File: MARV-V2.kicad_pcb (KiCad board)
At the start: 4 copper layers, 50.7 x 45.5 mm, 106 parts, among them J10 DBG pads (SWCLK SWDIO GND), J11 microSD, Molex 104031-0811 pu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, J3 ESC pads (CURR TX M4 M3 M2 M1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, J4 USB_C_PROGRAM_POWER, J6 IO array signal column (inner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, J7 IO array power column (5V / 3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, J8 IO array GND column (board ed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, Q1 AO3401A, SW1 RESET (RUN to GND), SW2 BOOTSEL (via R24), U12 TPS7A2033PDBVR, U20 RP2354B, U21 ICM-45686 6-axis IMU, U22 BMP581 barometer, U23 ADXL375 high-g accelerometer, U24 DNP: W25Q32JVSNIQ, 32 Mbit QS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, U7 AP63203WU-7, Y1 12 MHz TAXM12M4RFBCCT2T, CL 1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

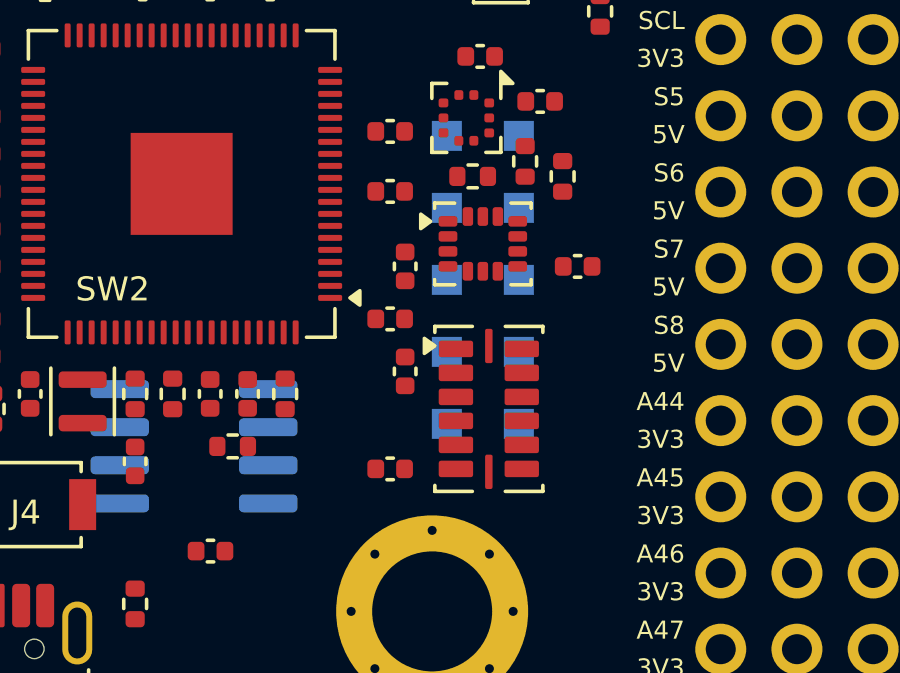
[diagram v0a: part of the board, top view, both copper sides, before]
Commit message: Save communication schematic, locking microSD and manual PCB updates
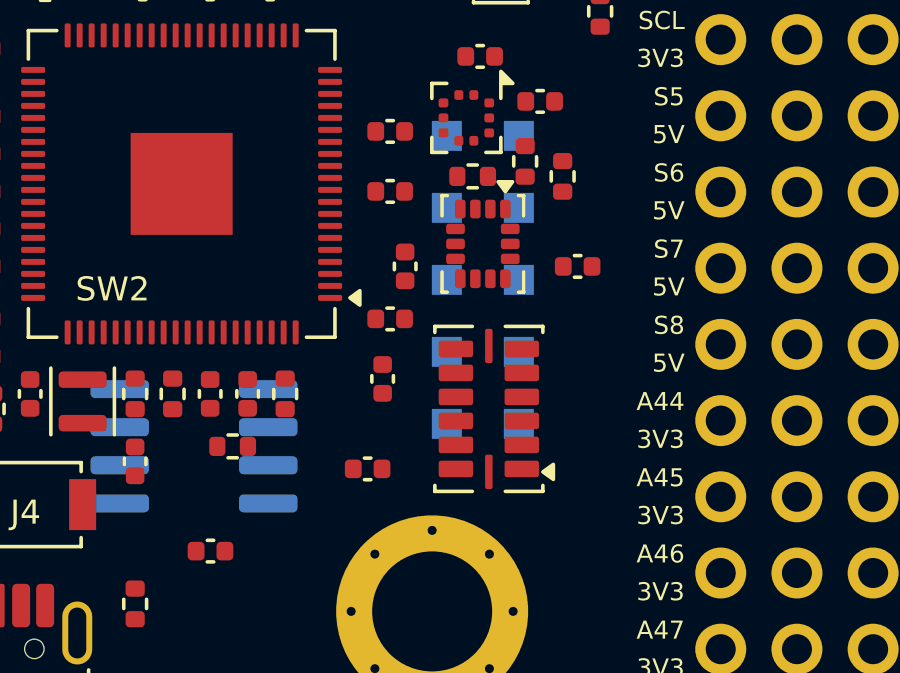
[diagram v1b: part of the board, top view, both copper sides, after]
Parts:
- moved C60 0.79 mm to (107.5, 107.5)
- moved C59 0.75 mm to (107.0, 110.5)
- turned U21 to -90 degrees
- turned U23 to 180 degrees
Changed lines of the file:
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@@
 	(footprint "Capacitor_SMD:C_0402_1005Metric"
 		(layer "F.Cu")
-		(at 108.25 107.25 -90)
+		(at 107.5 107.5 -90)
 		(descr "Capacitor SMD 0402 (1005 Metric), square (rectangular) end terminal, IPC-7351 nominal, (Body size source: IPC-SM-782 page 76, https://www.pcb-3d.com/wordpress/wp-content/uploads/ipc-sm-782a_amendment_1_and_2.pdf)")
 		(tags "capacitor")
@@
 		)
 		(embedded_fonts no)
-		(model "${KIPRJMOD}/MARV_Packages.3dshapes/microSD_HC_Molex_104031-0811.step"
+		(model "${KIPRJMOD}/MARV_Packages.3dshapes/microSD_HC_Molex_47219-2001.step"
 			(offset
-				(xyz 0.092 -0.3 1.4456)
+				(xyz -0.005 0 0)
 			)
 			(scale
@@
 			)
 			(rotate
-				(xyz -90 0 180)
+				(xyz 0 0 180)
 			)
 		)
@@
 	(footprint "MARV_Packages:InvenSense_LGA-14_2.5x3mm_P0.5mm_ICM45686"
 		(layer "F.Cu")
-		(at 110.84 103)
+		(at 110.84 103 -90)
 		(descr "TDK InvenSense ICM-45686 6-axis IMU, 14-pin LGA 2.5x3x0.81 mm, 0.5 mm pitch. Pad geometry identical to KiCad LGA-14_3x2.5mm_P0.5mm_LayoutBorder3x4y and verified by the lead against DS-000577 Rev 1.0 Sec 11.2 (page 52 TOP VIEW: pin 1 at top of the left edge, counterclockwise; side columns x=+/-1.1625, top/bottom rows y=+/-0.9125). 3D model is a dimensional stand-in copied from the KiCad generic LGA-14 STEP.")
 		(tags "InvenSense TDK ICM-45686 LGA-14 IMU accelerometer gyroscope")
 		(property "Reference" "U21"
-			(at 0 -2.2 0)
+			(at 0 -2.2 90)
 			(layer "F.SilkS")
 			(hide yes)
@@
 		)
 		(property "Value" "ICM-45686 6-axis IMU"
-			(at 0 2.2 0)
+			(at 0 2.2 90)
 			(layer "F.Fab")
 			(hide yes)
@@
 		)
 		(property "Datasheet" ""
-			(at 0 0 0)
+			(at 0 0 90)
 			(layer "F.Fab")
 			(hide yes)
@@
 		)
 		(property "Description" ""
-			(at 0 0 0)
+			(at 0 0 90)
 			(layer "F.Fab")
 			(hide yes)
@@
 		)
 		(property "KiLib_Generator" "package/no_lead"
-			(at 0 0 0)
+			(at 0 0 90)
 			(layer "F.SilkS")
 			(hide yes)
@@
 		(duplicate_pad_numbers_are_jumpers no)
 		(fp_line
-			(start -1.61 -1.36)
-			(end -0.935 -1.36)
+			(start -1.61 1.36)
+			(end -1.61 1.185)
 			(stroke
 				(width 0.12)
@@
 		)
 		(fp_line
-			(start -1.61 -1.185)
-			(end -1.61 -1.36)
+			(start -0.935 1.36)
+			(end -1.61 1.36)
 			(stroke
 				(width 0.12)
@@
 		)
 		(fp_line
-			(start -1.61 1.36)
-			(end -1.61 1.185)
+			(start 1.61 1.36)
+			(end 0.935 1.36)
 			(stroke
 				(width 0.12)
@@
 		)
 		(fp_line
-			(start -0.935 1.36)
-			(end -1.61 1.36)
+			(start 1.61 1.185)
+			(end 1.61 1.36)
 			(stroke
 				(width 0.12)
@@
 		)
 		(fp_line
-			(start 0.935 -1.36)
-			(end 1.61 -1.36)
+			(start -1.61 -1.185)
+			(end -1.61 -1.36)
 			(stroke
 				(width 0.12)
@@
 		)
 		(fp_line
-			(start 1.61 -1.36)
-			(end 1.61 -1.185)
+			(start -1.61 -1.36)
+			(end -0.935 -1.36)
 			(stroke
 				(width 0.12)
@@
 		)
 		(fp_line
-			(start 1.61 1.185)
-			(end 1.61 1.36)
+			(start 0.935 -1.36)
+			(end 1.61 -1.36)
 			(stroke
 				(width 0.12)
@@
 		)
 		(fp_line
-			(start 1.61 1.36)
-			(end 0.935 1.36)
+			(start 1.61 -1.36)
+			(end 1.61 -1.185)
 			(stroke
 				(width 0.12)
@@
 		)
 		(fp_text user "${REFERENCE}"
-			(at 0 0 0)
+			(at 0 0 90)
 			(layer "F.Fab")
 			(effects
@@
 		)
 		(pad "1" smd roundrect
-			(at -1.1625 -0.75)
+			(at -1.1625 -0.75 270)
 			(size 0.625 0.35)
 			(layers "F.Cu" "F.Mask" "F.Paste")
@@
 		)
 		(pad "2" smd roundrect
-			(at -1.1625 -0.25)
+			(at -1.1625 -0.25 270)
 			(size 0.625 0.35)
 			(layers "F.Cu" "F.Mask" "F.Paste")
@@
 		)
 		(pad "3" smd roundrect
-			(at -1.1625 0.25)
+			(at -1.1625 0.25 270)
 			(size 0.625 0.35)
 			(layers "F.Cu" "F.Mask" "F.Paste")
@@
 		)
 		(pad "4" smd roundrect
-			(at -1.1625 0.75)
+			(at -1.1625 0.75 270)
 			(size 0.625 0.35)
 			(layers "F.Cu" "F.Mask" "F.Paste")
@@
 		)
 		(pad "5" smd roundrect
-			(at -0.5 0.9125)
+			(at -0.5 0.9125 270)
 			(size 0.35 0.625)
 			(layers "F.Cu" "F.Mask" "F.Paste")
@@
 		)
 		(pad "6" smd roundrect
-			(at 0 0.9125)
+			(at 0 0.9125 270)
 			(size 0.35 0.625)
 			(layers "F.Cu" "F.Mask" "F.Paste")
@@
 		)
 		(pad "7" smd roundrect
-			(at 0.5 0.9125)
+			(at 0.5 0.9125 270)
 			(size 0.35 0.625)
 			(layers "F.Cu" "F.Mask" "F.Paste")
@@
 		)
 		(pad "8" smd roundrect
-			(at 1.1625 0.75)
+			(at 1.1625 0.75 270)
 			(size 0.625 0.35)
 			(layers "F.Cu" "F.Mask" "F.Paste")
@@
 		)
 		(pad "9" smd roundrect
-			(at 1.1625 0.25)
+			(at 1.1625 0.25 270)
 			(size 0.625 0.35)
 			(layers "F.Cu" "F.Mask" "F.Paste")
@@
 		)
 		(pad "10" smd roundrect
-			(at 1.1625 -0.25)
+			(at 1.1625 -0.25 270)
 			(size 0.625 0.35)
 			(layers "F.Cu" "F.Mask" "F.Paste")
@@
 		)
 		(pad "11" smd roundrect
-			(at 1.1625 -0.75)
+			(at 1.1625 -0.75 270)
 			(size 0.625 0.35)
 			(layers "F.Cu" "F.Mask" "F.Paste")
@@
 		)
 		(pad "12" smd roundrect
-			(at 0.5 -0.9125)
+			(at 0.5 -0.9125 270)
 			(size 0.35 0.625)
 			(layers "F.Cu" "F.Mask" "F.Paste")
@@
 		)
 		(pad "13" smd roundrect
-			(at 0 -0.9125)
+			(at 0 -0.9125 270)
 			(size 0.35 0.625)
 			(layers "F.Cu" "F.Mask" "F.Paste")
@@
 		)
 		(pad "14" smd roundrect
-			(at -0.5 -0.9125)
+			(at -0.5 -0.9125 270)
 			(size 0.35 0.625)
 			(layers "F.Cu" "F.Mask" "F.Paste")
@@
 	(footprint "MARV_Packages:Analog_LGA-14_3x5mm_P0.8mm_ADXL375"
 		(layer "F.Cu")
-		(at 111.039999 108.5)
+		(at 111.039999 108.5 180)
 		(descr "Analog Devices ADXL375, CC-14-1 14-terminal 3x5 mm LGA; datasheet recommended land pattern")
 		(tags "Analog Devices ADXL375 LGA-14 accelerometer")
@@
 		(duplicate_pad_numbers_are_jumpers no)
 		(fp_line
-			(start -1.8 -2.75)
-			(end -1.8 -2.55)
+			(start 1.8 2.75)
+			(end 1.8 2.55)
 			(stroke
 				(width 0.12)
@@
 		)
 		(fp_line
-			(start -1.8 -2.75)
-			(end -0.55 -2.75)
+			(start 1.8 -2.75)
+			(end 1.8 -2.55)
 			(stroke
 				(width 0.12)
@@
 		)
 		(fp_line
-			(start -1.8 2.75)
-			(end -1.8 2.55)
+			(start 0.55 2.75)
+			(end 1.8 2.75)
 			(stroke
 				(width 0.12)
@@
 		)
 		(fp_line
-			(start -1.8 2.75)
-			(end -0.55 2.75)
+			(start 0.55 -2.75)
+			(end 1.8 -2.75)
 			(stroke
 				(width 0.12)
@@
 		)
 		(fp_line
-			(start 0.55 -2.75)
-			(end 1.8 -2.75)
+			(start -1.8 2.75)
+			(end -0.55 2.75)
 			(stroke
 				(width 0.12)
@@
 		)
 		(fp_line
-			(start 0.55 2.75)
-			(end 1.8 2.75)
+			(start -1.8 2.75)
+			(end -1.8 2.55)
 			(stroke
 				(width 0.12)
@@
 		)
 		(fp_line
-			(start 1.8 -2.75)
-			(end 1.8 -2.55)
+			(start -1.8 -2.75)
+			(end -0.55 -2.75)
 			(stroke
 				(width 0.12)
@@
 		)
 		(fp_line
-			(start 1.8 2.75)
-			(end 1.8 2.55)
+			(start -1.8 -2.75)
+			(end -1.8 -2.55)
 			(stroke
 				(width 0.12)
@@
 		)
 		(pad "1" smd roundrect
-			(at -1.0975 -2)
+			(at -1.0975 -2 180)
 			(size 1.145 0.55)
 			(layers "F.Cu" "F.Mask" "F.Paste")
@@
 		)
 		(pad "2" smd roundrect
-			(at -1.0975 -1.2)
+			(at -1.0975 -1.2 180)
 			(size 1.145 0.55)
 			(layers "F.Cu" "F.Mask" "F.Paste")
@@
 		)
 		(pad "3" smd roundrect
-			(at -1.0975 -0.4)
+			(at -1.0975 -0.4 180)
 			(size 1.145 0.55)
 			(layers "F.Cu" "F.Mask" "F.Paste")
@@
 		)
 		(pad "4" smd roundrect
-			(at -1.0975 0.4)
+			(at -1.0975 0.4 180)
 			(size 1.145 0.55)
 			(layers "F.Cu" "F.Mask" "F.Paste")
@@
 		)
 		(pad "5" smd roundrect
-			(at -1.0975 1.2)
+			(at -1.0975 1.2 180)
 			(size 1.145 0.55)
 			(layers "F.Cu" "F.Mask" "F.Paste")
@@
 		)
 		(pad "6" smd roundrect
-			(at -1.0975 2)
+			(at -1.0975 2 180)
 			(size 1.145 0.55)
 			(layers "F.Cu" "F.Mask" "F.Paste")
@@
 		)
 		(pad "7" smd roundrect
-			(at 0 2.0975)
+			(at 0 2.0975 180)
 			(size 0.25 1.145)
 			(layers "F.Cu" "F.Mask" "F.Paste")
@@
 		)
 		(pad "8" smd roundrect
-			(at 1.0975 2)
+			(at 1.0975 2 180)
 			(size 1.145 0.55)
 			(layers "F.Cu" "F.Mask" "F.Paste")
@@
 		)
 		(pad "9" smd roundrect
-			(at 1.0975 1.2)
+			(at 1.0975 1.2 180)
 			(size 1.145 0.55)
 			(layers "F.Cu" "F.Mask" "F.Paste")
@@
 		)
 		(pad "10" smd roundrect
-			(at 1.0975 0.4)
+			(at 1.0975 0.4 180)
 			(size 1.145 0.55)
 			(layers "F.Cu" "F.Mask" "F.Paste")
@@
 		)
 		(pad "11" smd roundrect
-			(at 1.0975 -0.4)
+			(at 1.0975 -0.4 180)
 			(size 1.145 0.55)
 			(layers "F.Cu" "F.Mask" "F.Paste")
@@
 		)
 		(pad "12" smd roundrect
-			(at 1.0975 -1.2)
+			(at 1.0975 -1.2 180)
 			(size 1.145 0.55)
 			(layers "F.Cu" "F.Mask" "F.Paste")
@@
 		)
 		(pad "13" smd roundrect
-			(at 1.0975 -2)
+			(at 1.0975 -2 180)
 			(size 1.145 0.55)
 			(layers "F.Cu" "F.Mask" "F.Paste")
@@
 		)
 		(pad "14" smd roundrect
-			(at 0 -2.0975)
+			(at 0 -2.0975 180)
 			(size 0.25 1.145)
 			(layers "F.Cu" "F.Mask" "F.Paste")
@@
 	(footprint "Capacitor_SMD:C_0402_1005Metric"
 		(layer "F.Cu")
-		(at 107.75 110.5 180)
+		(at 107 110.5 180)
 		(descr "Capacitor SMD 0402 (1005 Metric), square (rectangular) end terminal, IPC-7351 nominal, (Body size source: IPC-SM-782 page 76, https://www.pcb-3d.com/wordpress/wp-content/uploads/ipc-sm-782a_amendment_1_and_2.pdf)")
 		(tags "capacitor")

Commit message: update
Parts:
- removed R41: 10k, SD_DET pull-up, Resistor_SMD:R_0402_1005Metric
- added R57: 4.7k, Resistor_SMD:R_0402_1005Metric, F.Cu at (108.9, 91.7)
- added R58: 22, Resistor_SMD:R_0402_1005Metric, F.Cu at (95.8, 94.8)
- C48: value 100n / 16 V X7R, ADC1 -> 100n / 16 V X7R, ADC2
- C78: value 100n / 16 V X7R, ADC2 filter -> 100n / 16 V X7R, ADC1 filter
- J11: value microSD, Molex 104031-0811 push-push -> microSD, Molex 47219-2001 locking hinge; footprint MARV_Packages:microSD_HC_Molex_104031-0811 -> MARV_Packages:microSD_HC_Molex_47219-2001
- R37: value 10k, SD_D0 pull-up -> 10k, SD_DAT0 pull-up
- R38: value 10k, SD_D1 pull-up -> 10k, SD_DAT1 pull-up
- R39: value 10k, SD_D2 pull-up -> 10k, SD_DAT2 pull-up
- R40: value 10k, SD_D3 pull-up -> 10k, SD_DAT3 pull-up
- R48: value 10k, IMU_CS pull-up -> 10k, ICM_CS pull-up
- R50: value 10k, BARO_CS pull-up -> 4.7k
- R51: value 10k, HG_ACC_CS pull-up -> 10k, ADXL_CS pull-up
- TP1: value TP SENS_SCK -> TP ICM_SCK
- TP10: value TP HG_ACC_INT -> TP ADXL_INT1
- TP2: value TP SENS_MOSI -> TP ICM_MOSI
- TP3: value TP SENS_MISO -> TP ICM_MISO
- TP4: value TP IMU_CS -> TP ICM_CS
- TP5: value TP BARO_CS -> TP BARO_SDA
- TP6: value TP HG_ACC_CS -> TP ADXL_CS
- TP7: value TP IMU_INT1 -> TP ICM_INT1
- TP8: value TP IMU_INT2 -> TP ICM_INT2
- moved J10 42.3 mm to (101.2, 78.8)
- moved SW1 32.6 mm to (103.5, 82.0), turned to 90 degrees
- moved C26 22.1 mm to (103.3, 110.8), turned to 180 degrees
- moved C25 21.9 mm to (100.3, 112.9), turned to -90 degrees
- moved U12 21.7 mm to (102.8, 113.3)
- moved R55 17.3 mm to (91.3, 108.3)
- moved C79 17.1 mm to (91.3, 107.3)
- moved D20 17.0 mm to (88.8, 107.8)
- moved R36 16.4 mm to (90.8, 94.1), turned to 180 degrees
- moved R39 15.2 mm to (85.5, 93.0), turned to 90 degrees
- moved R40 15.2 mm to (87.7, 93.0), turned to 90 degrees
- moved R50 10.2 mm to (108.9, 90.6), turned to 0 degrees
- moved C64 10.1 mm to (99.2, 81.5)
- moved C37 9.82 mm to (93.2, 109.2), turned to -135 degrees
- moved SW2 9.55 mm to (100.5, 120.0), turned to -90 degrees
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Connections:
- net HG_ACC_INT renamed ADXL_INT1
- net IMU_CS renamed ICM_CS
- net IMU_INT1 renamed ICM_INT1
- net SD_D0 renamed SD_DAT0
- net SD_D1 renamed SD_DAT1
- net SD_D2 renamed SD_DAT2
- net SD_D3 renamed SD_DAT3
- R50 pad 2: BARO_CS -> BARO_SCL
- R51 pad 2: HG_ACC_CS -> ADXL_CS
- TP1 pad 1: SENS_SCK -> ICM_SCK
- TP2 pad 1: SENS_MOSI -> ICM_MOSI
- TP3 pad 1: SENS_MISO -> ICM_MISO
- TP5 pad 1: BARO_CS -> BARO_SDA
- TP6 pad 1: HG_ACC_CS -> ADXL_CS
- TP8 pad 1: IMU_INT2 -> ICM_INT2
- U20 pad 1: HG_ACC_CS -> ADXL_MISO
- U20 pad 11: unconnected-(U20-GPIO12-Pad11) -> BARO_SDA
- U20 pad 13: BARO_CS -> ADXL_CS
- U20 pad 18: unconnected-(U20-GPIO18-Pad18) -> ICM_INT2
- U20 pad 21: unconnected-(U20-GPIO21-Pad21) -> ADXL_INT2
- U20 pad 40: ESC_TELEM_RX -> SD_CLK_MCU
- U20 pad 42: SD_CLK -> SD_CMD
- U20 pad 43: SD_CMD -> ESC_TELEM_RX
- U20 pad 44: SD_DET -> unconnected-(U20-GPIO35-Pad44)
- U20 pad 46: unconnected-(U20-GPIO37-Pad46) -> PWM3
- U20 pad 47: PWM3 -> PWM2
- U20 pad 48: PWM2 -> PWM1
- U20 pad 52: VBAT_SENSE -> CURR_SENSE
- U20 pad 53: CURR_SENSE -> VBAT_SENSE
- U20 pad 54: PWM1 -> LED_DATA
- U20 pad 6: SENS_MISO -> ICM_MISO
- U20 pad 7: unconnected-(U20-GPIO9-Pad7) -> BARO_SCL
- U20 pad 79: IMU_INT2 -> ADXL_SCK
- U20 pad 8: SENS_SCK -> ICM_SCK
- U20 pad 80: LED_DATA -> ADXL_MOSI
- U20 pad 9: SENS_MOSI -> ICM_MOSI
- U21 pad 1: SENS_MISO -> ICM_MISO
- U21 pad 13: SENS_SCK -> ICM_SCK
- U21 pad 14: SENS_MOSI -> ICM_MOSI
- U21 pad 9: IMU_INT2 -> ICM_INT2
- U22 pad 2: SENS_SCK -> BARO_SCL
- U22 pad 4: SENS_MOSI -> BARO_SDA
- U22 pad 5: SENS_MISO -> GND
- U22 pad 6: BARO_CS -> V3V3_ANA
- U23 pad 12: SENS_MISO -> ADXL_MISO
- U23 pad 13: SENS_MOSI -> ADXL_MOSI
- U23 pad 14: SENS_SCK -> ADXL_SCK
- U23 pad 7: HG_ACC_CS -> ADXL_CS
- U23 pad 9: unconnected-(U23-INT2-Pad9) -> ADXL_INT2
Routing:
- net USB_VBUS: track 0.00 -> 39.0 mm
- net PWM3: track 0.00 -> 21.2 mm, vias 0 -> 1
- net PWM2: track 0.00 -> 21.0 mm, vias 0 -> 1
- net SD_DAT1: track 0.00 -> 20.9 mm, vias 0 -> 2
- net SD_DAT0: track 0.00 -> 20.8 mm
- net PWM4: track 0.00 -> 20.8 mm, vias 0 -> 1
- net PWM1: track 0.00 -> 20.7 mm, vias 0 -> 1
- net SWDIO: track 0.00 -> 19.5 mm, vias 0 -> 1
- net CURR_SENSE_RAW: track 0.00 -> 19.4 mm, vias 0 -> 3
- net SWCLK: track 0.00 -> 18.8 mm, vias 0 -> 1
- net V5_SYS: track 0.00 -> 18.6 mm, vias 0 -> 2
- net SD_DAT2: track 0.00 -> 18.1 mm
- net SD_DAT3: track 0.00 -> 17.7 mm, vias 0 -> 2
- net ESC_TELEM: track 0.00 -> 17.7 mm, vias 0 -> 1
- net MCU_RUN: track 0.00 -> 16.2 mm
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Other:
- board text removed: "MARV V2"

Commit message: routing
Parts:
- moved R51 3.48 mm to (112.8, 104.2), turned to 180 degrees
- moved C26 2.19 mm to (105.5, 111.0), turned to 0 degrees
- moved R39 1.61 mm to (87.1, 92.9)
- moved R36 1.36 mm to (90.0, 93.0), turned to 90 degrees
- moved R40 0.86 mm to (88.5, 92.9)
- moved C33 0.35 mm to (102.0, 94.3)
- moved R35 0.32 mm to (100.7, 111.2)
- moved C41 0.18 mm to (96.3, 108.0)
- moved R20 0.18 mm to (95.6, 107.2)
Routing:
- net GND: track 0.00 -> 24.5 mm, vias 1 -> 26
- net DVDD: track 6.36 -> 29.5 mm
- net SD_CMD: track 0.00 -> 18.3 mm, vias 0 -> 2
- net V5_SYS: track 18.6 -> 32.3 mm, vias 2 -> 3
- net V3V3_SYS: track 15.1 -> 27.9 mm
- net SD_DAT2: track 18.1 -> 25.2 mm
- net SD_DAT3: track 17.7 -> 23.5 mm
- net VREG_AVDD: track 0.00 -> 2.43 mm
- net V3V3_ANA: track 1.38 -> 3.03 mm
- net VBAT: track 15.5 -> 16.2 mm
- added copper zone on In1.Cu, net GND
- added copper zone on In2.Cu, net V3V3_SYS

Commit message: finished routing
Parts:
- moved TP7 9.77 mm to (112.6, 96.8)
- moved TP9 9.10 mm to (105.8, 98.3)
- moved R25 8.62 mm to (116.4, 92.5), turned to 0 degrees
- moved R26 8.48 mm to (116.4, 95.2), turned to 0 degrees
- moved TP3 6.90 mm to (115.2, 97.7)
- moved TP6 6.78 mm to (110.1, 102.5)
- moved TP4 6.74 mm to (116.2, 102.7)
- moved TP5 6.40 mm to (104.8, 95.2)
- moved TP2 5.65 mm to (107.9, 100.3)
- moved TP1 4.64 mm to (116.2, 99.7)
- moved C56 4.00 mm to (110.9, 93.9), turned to -90 degrees
- moved TP10 3.37 mm to (110.8, 105.8)
- moved C37 2.69 mm to (94.9, 107.0)
- moved TP8 2.35 mm to (112.2, 101.8)
- moved R50 2.34 mm to (111.2, 90.0), turned to 180 degrees
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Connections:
- J7 pad 10: 5V_IN -> V3V3_SYS
- J7 pad 7: 5V_IN -> V3V3_SYS
- J7 pad 8: 5V_IN -> V3V3_SYS
- J7 pad 9: 5V_IN -> V3V3_SYS
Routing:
- net V3V3_ANA: track 3.03 -> 86.9 mm, vias 0 -> 9
- net GND: track 24.5 -> 85.9 mm, vias 26 -> 71
- net V3V3_SYS: track 27.9 -> 69.0 mm, vias 0 -> 24
- net IO_GPIO46: track 0.00 -> 29.3 mm, vias 0 -> 1
- net IO_GPIO47: track 0.00 -> 28.3 mm, vias 0 -> 1
- net IO_GPIO45: track 0.00 -> 26.6 mm, vias 0 -> 1
- net IO_GPIO44: track 0.00 -> 26.0 mm, vias 0 -> 1
- net PWM7: track 0.00 -> 24.0 mm, vias 0 -> 1
- net GPS_RX: track 0.00 -> 21.6 mm
- net GPS_TX: track 0.00 -> 21.1 mm, vias 0 -> 1
- net ICM_MISO: track 0.00 -> 20.4 mm, vias 0 -> 2
- net MAG_SCL: track 0.00 -> 19.2 mm, vias 0 -> 1
- net MAG_SDA: track 0.00 -> 18.4 mm, vias 0 -> 1
- net BARO_SCL: track 0.00 -> 18.3 mm, vias 0 -> 2
- net BARO_INT: track 0.00 -> 18.0 mm, vias 0 -> 4
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- added copper zone on F.Cu, net GND
